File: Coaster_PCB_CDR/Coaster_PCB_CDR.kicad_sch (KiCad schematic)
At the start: 31 parts, among them J1 Vin, J10 GND, J11 GND, J12 GND, J13 3v3, J14 GND, J15 GND, J2 HC-05, J3 10V, J4 Batt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

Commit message: Updated CDR PCB more
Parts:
- removed Z1: Zener, digikey-footprints:DO-214AC, symbol M5_BuggyProject-rescue:1N5231BTR-dk_Diodes-Zener-Single
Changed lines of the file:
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@@
     (pin "2")
-  )
-  (symbol (lib_id "power:GND") (at 91.44 48.26 0) (unit 1)
-    (in_bom yes) (on_board yes)
-    (property "Reference" "#PWR06" (id 0) (at 91.44 54.61 0)
-      (effects (font (size 1.27 1.27)) hide)
-    )
-    (property "Value" "GND" (id 1) (at 91.567 52.6542 0))
-    (property "Footprint" "" (id 2) (at 91.44 48.26 0)
-      (effects (font (size 1.27 1.27)) hide)
-    )
-    (property "Datasheet" "" (id 3) (at 91.44 48.26 0)
-      (effects (font (size 1.27 1.27)) hide)
-    )
-    (pin "1")
   )
   (symbol (lib_id "Device:R") (at 97.79 38.1 270) (unit 1)
@@
     (pin "1")
     (pin "2")
-  )
-  (symbol (lib_id "M5_BuggyProject-rescue:1N5231BTR-dk_Diodes-Zener-Single") (at 91.44 43.18 90) (unit 1)
-    (in_bom yes) (on_board yes)
-    (property "Reference" "Z1" (id 0) (at 93.4212 42.0116 90)
-      (effects (font (size 1.27 1.27)) (justify right))
-    )
-    (property "Value" "Zener" (id 1) (at 93.4212 44.323 90)
-      (effects (font (size 1.27 1.27)) (justify right))
-    )
-    (property "Footprint" "digikey-footprints:DO-214AC" (id 2) (at 86.36 38.1 0)
-      (effects (font (size 1.524 1.524)) (justify left) hide)
-    )
-    (property "Datasheet" "https://www.onsemi.com/pub/Collateral/1N5221B-D.PDF" (id 3) (at 83.82 38.1 0)
-      (effects (font (size 1.524 1.524)) (justify left) hide)
-    )
-    (property "Digi-Key_PN" "1N5231BFSCT-ND" (id 4) (at 81.28 38.1 0)
-      (effects (font (size 1.524 1.524)) (justify left) hide)
-    )
-    (property "MPN" "1N5231BTR" (id 5) (at 78.74 38.1 0)
-      (effects (font (size 1.524 1.524)) (justify left) hide)
-    )
-    (property "Category" "Discrete Semiconductor Products" (id 6) (at 76.2 38.1 0)
-      (effects (font (size 1.524 1.524)) (justify left) hide)
-    )
-    (property "Family" "Diodes - Zener - Single" (id 7) (at 73.66 38.1 0)
-      (effects (font (size 1.524 1.524)) (justify left) hide)
-    )
-    (property "DK_Datasheet_Link" "https://www.onsemi.com/pub/Collateral/1N5221B-D.PDF" (id 8) (at 71.12 38.1 0)
-      (effects (font (size 1.524 1.524)) (justify left) hide)
-    )
-    (property "DK_Detail_Page" "/product-detail/en/on-semiconductor/1N5231BTR/1N5231BFSCT-ND/1532765" (id 9) (at 68.58 38.1 0)
-      (effects (font (size 1.524 1.524)) (justify left) hide)
-    )
-    (property "Description" "DIODE ZENER 5.1V 500MW DO35" (id 10) (at 66.04 38.1 0)
-      (effects (font (size 1.524 1.524)) (justify left) hide)
-    )
-    (property "Manufacturer" "ON Semiconductor" (id 11) (at 63.5 38.1 0)
-      (effects (font (size 1.524 1.524)) (justify left) hide)
-    )
-    (property "Status" "Active" (id 12) (at 60.96 38.1 0)
-      (effects (font (size 1.524 1.524)) (justify left) hide)
-    )
-    (pin "A")
-    (pin "K")
   )
   (symbol (lib_id "power:VCC") (at 38.1 38.1 0) (unit 1)
@@
       (reference "#PWR05") (unit 1) (value "GND") (footprint "")
     )
-    (path "/00000000-0000-0000-0000-000061ddcf3d"
-      (reference "#PWR06") (unit 1) (value "GND") (footprint "")
-    )
     (path "/00000000-0000-0000-0000-000061e018c8"
       (reference "#PWR07") (unit 1) (value "GND") (footprint "")
@@
       (reference "U2") (unit 1) (value "Voltage Regulator") (footprint "Package_TO_SOT_THT:TO-220-3_Vertical")
     )
-    (path "/00000000-0000-0000-0000-000061df337e"
-      (reference "Z1") (unit 1) (value "Zener") (footprint "digikey-footprints:DO-214AC")
-    )
-  )
+  )

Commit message: Added some extra ground pins
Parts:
- added J16, J17: GND, Connector_PinSocket_2.54mm:PinSocket_1x02_P2.54mm_Vertical, symbol Connector_Generic:Conn_01x02
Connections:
- net GND: now also J16.1 (Pin_1), J16.2 (Pin_2), J17.1 (Pin_1), J17.2 (Pin_2)
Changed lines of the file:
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@@
+    (stroke (width 0) (type default) (color 0 0 0 0))
+  )
+  (wire (pts (xy 123.19 111.76) (xy 124.46 111.76))
     (stroke (width 0) (type default) (color 0 0 0 0))
   )
@@
     (stroke (width 0) (type default) (color 0 0 0 0))
   )
+  (wire (pts (xy 114.3 111.76) (xy 113.03 111.76))
+    (stroke (width 0) (type default) (color 0 0 0 0))
+  )
   (polyline (pts (xy 88.9 88.9) (xy 184.15 88.9))
     (stroke (width 0) (type default) (color 0 0 0 0))
@@
     (stroke (width 0) (type default) (color 0 0 0 0))
   )
+  (wire (pts (xy 109.22 111.76) (xy 110.49 111.76))
+    (stroke (width 0) (type default) (color 0 0 0 0))
+  )
   (wire (pts (xy 219.71 80.01) (xy 219.71 83.82))
     (stroke (width 0) (type default) (color 0 0 0 0))
@@
   )
   (wire (pts (xy 124.46 140.97) (xy 124.46 143.51))
+    (stroke (width 0) (type default) (color 0 0 0 0))
+  )
+  (wire (pts (xy 128.27 111.76) (xy 127 111.76))
     (stroke (width 0) (type default) (color 0 0 0 0))
   )
@@
     )
     (property "Datasheet" "" (id 3) (at 154.94 140.97 0)
+      (effects (font (size 1.27 1.27)) hide)
+    )
+    (pin "1")
+  )
+  (symbol (lib_id "power:GND") (at 123.19 111.76 180) (unit 1)
+    (in_bom yes) (on_board yes)
+    (property "Reference" "#PWR0135" (id 0) (at 123.19 105.41 0)
+      (effects (font (size 1.27 1.27)) hide)
+    )
+    (property "Value" "GND" (id 1) (at 123.063 107.3658 0))
+    (property "Footprint" "" (id 2) (at 123.19 111.76 0)
+      (effects (font (size 1.27 1.27)) hide)
+    )
+    (property "Datasheet" "" (id 3) (at 123.19 111.76 0)
       (effects (font (size 1.27 1.27)) hide)
     )
@@
     (pin "1")
   )
+  (symbol (lib_id "Connector_Generic:Conn_01x02") (at 127 116.84 270) (unit 1)
+    (in_bom yes) (on_board yes)
+    (property "Reference" "J17" (id 0) (at 129.54 115.5699 90)
+      (effects (font (size 1.27 1.27)) (justify left))
+    )
+    (property "Value" "GND" (id 1) (at 124.46 119.38 90)
+      (effects (font (size 1.27 1.27)) (justify left))
+    )
+    (property "Footprint" "Connector_PinSocket_2.54mm:PinSocket_1x02_P2.54mm_Vertical" (id 2) (at 127 116.84 0)
+      (effects (font (size 1.27 1.27)) hide)
+    )
+    (property "Datasheet" "~" (id 3) (at 127 116.84 0)
+      (effects (font (size 1.27 1.27)) hide)
+    )
+    (pin "1")
+    (pin "2")
+  )
   (symbol (lib_id "power:GND") (at 153.67 96.52 180) (unit 1)
     (in_bom yes) (on_board yes)
@@
     (pin "1")
   )
+  (symbol (lib_id "Connector_Generic:Conn_01x02") (at 113.03 116.84 270) (unit 1)
+    (in_bom yes) (on_board yes)
+    (property "Reference" "J16" (id 0) (at 115.57 115.5699 90)
+      (effects (font (size 1.27 1.27)) (justify left))
+    )
+    (property "Value" "GND" (id 1) (at 110.49 119.38 90)
+      (effects (font (size 1.27 1.27)) (justify left))
+    )
+    (property "Footprint" "Connector_PinSocket_2.54mm:PinSocket_1x02_P2.54mm_Vertical" (id 2) (at 113.03 116.84 0)
+      (effects (font (size 1.27 1.27)) hide)
+    )
+    (property "Datasheet" "~" (id 3) (at 113.03 116.84 0)
+      (effects (font (size 1.27 1.27)) hide)
+    )
+    (pin "1")
+    (pin "2")
+  )
   (symbol (lib_id "Connector_Generic:Conn_01x01") (at 119.38 101.6 270) (unit 1)
     (in_bom yes) (on_board yes)
@@
     )
     (property "Datasheet" "" (id 3) (at 170.18 33.02 0)
+      (effects (font (size 1.27 1.27)) hide)
+    )
+    (pin "1")
+  )
+  (symbol (lib_id "power:GND") (at 128.27 111.76 180) (unit 1)
+    (in_bom yes) (on_board yes)
+    (property "Reference" "#PWR0134" (id 0) (at 128.27 105.41 0)
+      (effects (font (size 1.27 1.27)) hide)
+    )
+    (property "Value" "GND" (id 1) (at 128.143 107.3658 0))
+    (property "Footprint" "" (id 2) (at 128.27 111.76 0)
+      (effects (font (size 1.27 1.27)) hide)
+    )
+    (property "Datasheet" "" (id 3) (at 128.27 111.76 0)
       (effects (font (size 1.27 1.27)) hide)
     )
@@
     (pin "7")
     (pin "8")
+  )
+  (symbol (lib_id "power:GND") (at 109.22 111.76 180) (unit 1)
+    (in_bom yes) (on_board yes)
+    (property "Reference" "#PWR0136" (id 0) (at 109.22 105.41 0)
+      (effects (font (size 1.27 1.27)) hide)
+    )
+    (property "Value" "GND" (id 1) (at 109.093 107.3658 0))
+    (property "Footprint" "" (id 2) (at 109.22 111.76 0)
+      (effects (font (size 1.27 1.27)) hide)
+    )
+    (property "Datasheet" "" (id 3) (at 109.22 111.76 0)
+      (effects (font (size 1.27 1.27)) hide)
+    )
+    (pin "1")
   )
   (symbol (lib_id "power:GND") (at 48.26 43.18 0) (unit 1)
@@
     (pin "1")
   )
+  (symbol (lib_id "power:GND") (at 114.3 111.76 180) (unit 1)
+    (in_bom yes) (on_board yes)
+    (property "Reference" "#PWR0133" (id 0) (at 114.3 105.41 0)
+      (effects (font (size 1.27 1.27)) hide)
+    )
+    (property "Value" "GND" (id 1) (at 114.173 107.3658 0))
+    (property "Footprint" "" (id 2) (at 114.3 111.76 0)
+      (effects (font (size 1.27 1.27)) hide)
+    )
+    (property "Datasheet" "" (id 3) (at 114.3 111.76 0)
+      (effects (font (size 1.27 1.27)) hide)
+    )
+    (pin "1")
+  )
   (symbol (lib_id "power:GND") (at 34.29 113.03 270) (unit 1)
     (in_bom yes) (on_board yes)
@@
       (reference "#PWR0132") (unit 1) (value "GND") (footprint "")
     )
+    (path "/ebbb1530-9016-4750-9e78-9109c2b98b54"
+      (reference "#PWR0133") (unit 1) (value "GND") (footprint "")
+    )
+    (path "/79ed7042-6307-4f8c-9088-8ee00e0acf30"
+      (reference "#PWR0134") (unit 1) (value "GND") (footprint "")
+    )
+    (path "/0e757eb5-d50e-4936-9516-2646da001ad2"
+      (reference "#PWR0135") (unit 1) (value "GND") (footprint "")
+    )
+    (path "/87fd98d3-d941-4e3b-b22d-da2d2f5663c5"
+      (reference "#PWR0136") (unit 1) (value "GND") (footprint "")
+    )
     (path "/00000000-0000-0000-0000-000061dd9ea3"
       (reference "C1") (unit 1) (value "2200uF") (footprint "Capacitor_THT:CP_Radial_D10.0mm_P5.00mm")
@@
       (reference "J15") (unit 1) (value "GND") (footprint "TestPoint:TestPoint_Plated_Hole_D5.0mm")
     )
+    (path "/625971dc-2c14-4501-889d-177b78e19c08"
+      (reference "J16") (unit 1) (value "GND") (footprint "Connector_PinSocket_2.54mm:PinSocket_1x02_P2.54mm_Vertical")
+    )
+    (path "/543552f1-c01b-41d0-8bfb-8a301b0c9979"
+      (reference "J17") (unit 1) (value "GND") (footprint "Connector_PinSocket_2.54mm:PinSocket_1x02_P2.54mm_Vertical")
+    )
     (path "/00000000-0000-0000-0000-000061d32985"

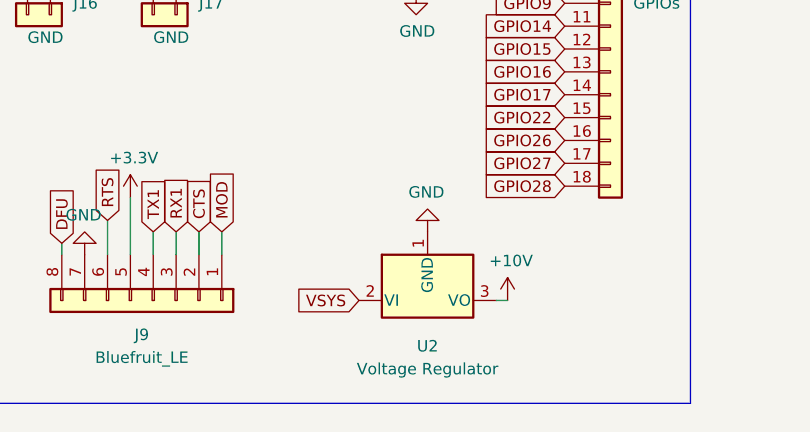
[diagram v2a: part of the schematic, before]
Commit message: fixed overlapping zones
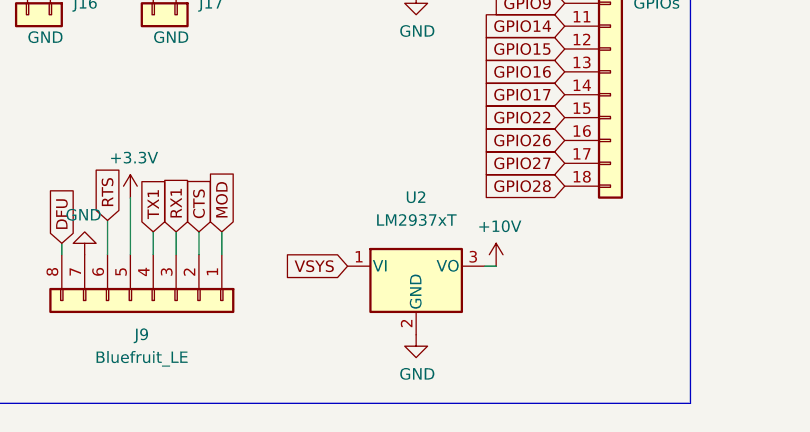
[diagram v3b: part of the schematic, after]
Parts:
- removed U2: Voltage Regulator, Package_TO_SOT_THT:TO-220-3_Vertical, symbol Regulator_Linear:MC79M15_TO220
- added U2: LM2937xT, Package_TO_SOT_THT:TO-220-3_Vertical, symbol Regulator_Linear:LM2937xT
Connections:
- net +10V: now also U2.3 (VO)
- net GND: now also U2.2 (GND)
- net VSYS: now also U2.1 (VI)
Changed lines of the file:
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@@
-    (stroke (width 0) (type default) (color 0 0 0 0))
-  )
-  (wire (pts (xy 163.83 148.59) (xy 162.56 148.59))
     (stroke (width 0) (type default) (color 0 0 0 0))
   )
@@
   )
   (wire (pts (xy 29.21 133.35) (xy 34.29 133.35))
+    (stroke (width 0) (type default) (color 0 0 0 0))
+  )
+  (wire (pts (xy 162.56 144.78) (xy 161.29 144.78))
     (stroke (width 0) (type default) (color 0 0 0 0))
   )
@@
     )
   )
+  (global_label "VSYS" (shape input) (at 146.05 144.78 180) (fields_autoplaced)
+    (effects (font (size 1.27 1.27)) (justify right))
+    (property "Intersheet References" "${INTERSHEET_REFS}" (id 0) (at 139.0407 144.7006 0)
+      (effects (font (size 1.27 1.27)) (justify right) hide)
+    )
+  )
   (global_label "GPIO17" (shape input) (at 77.47 149.86 270) (fields_autoplaced)
     (effects (font (size 1.27 1.27)) (justify right))
@@
     (property "Intersheet References" "${INTERSHEET_REFS}" (id 0) (at 132.0006 134.505 90)
       (effects (font (size 1.27 1.27)) (justify left) hide)
-    )
-  )
-  (global_label "VSYS" (shape input) (at 147.32 148.59 180) (fields_autoplaced)
-    (effects (font (size 1.27 1.27)) (justify right))
-    (property "Intersheet References" "${INTERSHEET_REFS}" (id 0) (at 140.3107 148.5106 0)
-      (effects (font (size 1.27 1.27)) (justify right) hide)
     )
   )
@@
     )
     (property "Datasheet" "" (id 3) (at 58.42 35.56 0)
-      (effects (font (size 1.27 1.27)) hide)
-    )
-    (pin "1")
-  )
-  (symbol (lib_id "power:GND") (at 154.94 140.97 180) (unit 1)
-    (in_bom yes) (on_board yes)
-    (property "Reference" "#PWR0122" (id 0) (at 154.94 134.62 0)
-      (effects (font (size 1.27 1.27)) hide)
-    )
-    (property "Value" "GND" (id 1) (at 154.813 136.5758 0))
-    (property "Footprint" "" (id 2) (at 154.94 140.97 0)
-      (effects (font (size 1.27 1.27)) hide)
-    )
-    (property "Datasheet" "" (id 3) (at 154.94 140.97 0)
       (effects (font (size 1.27 1.27)) hide)
     )
@@
     (pin "2")
   )
-  (symbol (lib_id "Regulator_Linear:MC79M15_TO220") (at 154.94 148.59 0) (unit 1)
-    (in_bom yes) (on_board yes) (fields_autoplaced)
-    (property "Reference" "U2" (id 0) (at 154.94 153.67 0))
-    (property "Value" "Voltage Regulator" (id 1) (at 154.94 156.21 0))
-    (property "Footprint" "Package_TO_SOT_THT:TO-220-3_Vertical" (id 2) (at 154.94 153.67 0)
-      (effects (font (size 1.27 1.27) italic) hide)
-    )
-    (property "Datasheet" "http://www.onsemi.com/pub/Collateral/MC79M00-D.PDF" (id 3) (at 154.94 148.59 0)
-      (effects (font (size 1.27 1.27)) hide)
-    )
-    (pin "1")
-    (pin "2")
-    (pin "3")
-  )
   (symbol (lib_id "power:GND") (at 146.05 96.52 180) (unit 1)
     (in_bom yes) (on_board yes)
@@
     (pin "1")
   )
+  (symbol (lib_id "power:GND") (at 153.67 152.4 0) (unit 1)
+    (in_bom yes) (on_board yes)
+    (property "Reference" "#PWR0122" (id 0) (at 153.67 158.75 0)
+      (effects (font (size 1.27 1.27)) hide)
+    )
+    (property "Value" "GND" (id 1) (at 153.797 156.7942 0))
+    (property "Footprint" "" (id 2) (at 153.67 152.4 0)
+      (effects (font (size 1.27 1.27)) hide)
+    )
+    (property "Datasheet" "" (id 3) (at 153.67 152.4 0)
+      (effects (font (size 1.27 1.27)) hide)
+    )
+    (pin "1")
+  )
   (symbol (lib_id "power:GND") (at 137.16 96.52 180) (unit 1)
     (in_bom yes) (on_board yes)
@@
     )
     (property "Datasheet" "" (id 3) (at 137.16 96.52 0)
+      (effects (font (size 1.27 1.27)) hide)
+    )
+    (pin "1")
+  )
+  (symbol (lib_id "power:+10V") (at 162.56 144.78 0) (unit 1)
+    (in_bom yes) (on_board yes)
+    (property "Reference" "#PWR0123" (id 0) (at 162.56 148.59 0)
+      (effects (font (size 1.27 1.27)) hide)
+    )
+    (property "Value" "+10V" (id 1) (at 162.941 140.3858 0))
+    (property "Footprint" "" (id 2) (at 162.56 144.78 0)
+      (effects (font (size 1.27 1.27)) hide)
+    )
+    (property "Datasheet" "" (id 3) (at 162.56 144.78 0)
       (effects (font (size 1.27 1.27)) hide)
     )
@@
     )
     (pin "1")
+  )
+  (symbol (lib_id "Regulator_Linear:LM2937xT") (at 153.67 144.78 0) (unit 1)
+    (in_bom yes) (on_board yes) (fields_autoplaced)
+    (property "Reference" "U2" (id 0) (at 153.67 137.16 0))
+    (property "Value" "LM2937xT" (id 1) (at 153.67 139.7 0))
+    (property "Footprint" "Package_TO_SOT_THT:TO-220-3_Vertical" (id 2) (at 153.67 139.065 0)
+      (effects (font (size 1.27 1.27) italic) hide)
+    )
+    (property "Datasheet" "http://www.ti.com/lit/ds/symlink/lm2937.pdf" (id 3) (at 153.67 146.05 0)
+      (effects (font (size 1.27 1.27)) hide)
+    )
+    (pin "1")
+    (pin "2")
+    (pin "3")
   )
   (symbol (lib_id "power:GND") (at 34.29 125.73 270) (unit 1)
@@
     (pin "1")
   )
-  (symbol (lib_id "power:+10V") (at 163.83 148.59 0) (unit 1)
-    (in_bom yes) (on_board yes)
-    (property "Reference" "#PWR0123" (id 0) (at 163.83 152.4 0)
-      (effects (font (size 1.27 1.27)) hide)
-    )
-    (property "Value" "+10V" (id 1) (at 164.211 144.1958 0))
-    (property "Footprint" "" (id 2) (at 163.83 148.59 0)
-      (effects (font (size 1.27 1.27)) hide)
-    )
-    (property "Datasheet" "" (id 3) (at 163.83 148.59 0)
-      (effects (font (size 1.27 1.27)) hide)
-    )
-    (pin "1")
-  )
   (symbol (lib_id "power:GND") (at 114.3 111.76 180) (unit 1)
     (in_bom yes) (on_board yes)
@@
       (reference "#PWR0121") (unit 1) (value "GND") (footprint "")
     )
-    (path "/0ab323da-06dc-4821-92c0-e44483d98e63"
+    (path "/38fa52b0-506c-432a-b23e-d0fb47dbb888"
       (reference "#PWR0122") (unit 1) (value "GND") (footprint "")
     )
-    (path "/e78f378c-0eb5-422d-a97b-1a258cdab9e2"
+    (path "/45922452-960c-4787-a2b2-e8abd71be39e"
       (reference "#PWR0123") (unit 1) (value "+10V") (footprint "")
     )
@@
       (reference "U1") (unit 1) (value "PicoW") (footprint "RPi_Pico:RPi_PicoW_SMD_TH")
     )
-    (path "/252bb8d6-5d41-4d75-bf5f-fe32aebab8f1"
-      (reference "U2") (unit 1) (value "Voltage Regulator") (footprint "Package_TO_SOT_THT:TO-220-3_Vertical")
-    )
-  )
+    (path "/9a1e93dd-bcd8-4f4f-bb33-c231142f3f81"
+      (reference "U2") (unit 1) (value "LM2937xT") (footprint "Package_TO_SOT_THT:TO-220-3_Vertical")
+    )
+  )

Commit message: changed pcb
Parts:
- removed J10, J11, J12, J14, J15, J5: GND, TestPoint:TestPoint_Plated_Hole_D5.0mm, symbol Connector_Generic:Conn_01x01
- removed J9: Bluefruit_LE, Connector_PinSocket_2.54mm:PinSocket_1x08_P2.54mm_Vertical, symbol Connector_Generic:Conn_01x08
- added J18, J19: 5v, Connector_PinSocket_2.54mm:PinSocket_1x02_P2.54mm_Vertical, symbol Connector_Generic:Conn_01x02
- added J9: 3v3, Connector_PinSocket_2.54mm:PinSocket_1x02_P2.54mm_Vertical, symbol Connector_Generic:Conn_01x02
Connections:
- net +3V3: now also J9.1 (Pin_1); no longer J2.2 (Pin_2)
- net GND: now also J18.2 (Pin_2), J19.2 (Pin_2), J9.2 (Pin_2); no longer H1.1, H2.1, H3.1, H4.1
- net GPIO16: now also J2.4 (Pin_4); no longer J2.5 (Pin_5)
- net GPIO17: now also J2.5 (Pin_5); no longer J2.4 (Pin_4)
- net +10V renamed vBatt
- net vBatt: now also U2.1 (VI); no longer U2.3 (VO)
- net VSYS renamed +5V
- net +5V: now also J2.2 (Pin_2), U2.3 (VO), J18.1 (Pin_1), J19.1 (Pin_1); no longer U2.1 (VI)
- net Vcc_10v renamed VCC_Batt
- no-connect marks 8 -> 12

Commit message: Updated PCB for FDR
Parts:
- removed J16, J17: GND, Connector_PinSocket_2.54mm:PinSocket_1x02_P2.54mm_Vertical, symbol Connector_Generic:Conn_01x02
- removed J8: GPIOs, Connector_PinSocket_2.54mm:PinSocket_1x18_P2.54mm_Vertical, symbol Connector_Generic:Conn_01x18
- added J10: Batt, Connector_PinSocket_2.54mm:PinSocket_1x02_P2.54mm_Vertical, symbol Connector_Generic:Conn_01x02
- added J11: GPIO_14-15, Connector_PinSocket_2.54mm:PinSocket_1x02_P2.54mm_Vertical, symbol Connector_Generic:Conn_01x02
- added J12: GPIO_27-28, Connector_PinSocket_2.54mm:PinSocket_1x02_P2.54mm_Vertical, symbol Connector_Generic:Conn_01x02
- added J5: HC-05, Connector_PinSocket_2.54mm:PinSocket_1x06_P2.54mm_Vertical, symbol Connector_Generic:Conn_01x06
- added J8: GPIO_0-1, Connector_PinSocket_2.54mm:PinSocket_1x02_P2.54mm_Vertical, symbol Connector_Generic:Conn_01x02
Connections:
- net +5V: now also J10.1 (Pin_1), J5.2 (Pin_2)
- net GND: now also J10.2 (Pin_2), J5.3 (Pin_3)
- net GPIO1: now also J8.2 (Pin_2)
- net GPIO15: now also J11.2 (Pin_2)
- net GPIO16: now also J5.4 (Pin_4)
- net GPIO17: now also J5.5 (Pin_5)
- net GPIO27: now also J12.1 (Pin_1)
- net GPIO28: now also J12.2 (Pin_2)
- net CTS renamed GPIO14
- net GPIO14: now also J11.1 (Pin_1)
- net DFU renamed GPIO0
- net GPIO0: now also J8.1 (Pin_1)
- no-connect marks 12 -> 14
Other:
- moved on the sheet: J13, J18, J19, J3, J7, U2
